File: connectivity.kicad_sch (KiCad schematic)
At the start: 28 parts, among them J10 Screw_Terminal_01x05, J11 RJ45_Hanrun_HR911105A_Horizon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, J8 Conn_02x01, J9 Conn_02x01, U10 LAN8742A, U9 TJA1042T-3, Y3 25 MHz

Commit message: Initial release A1
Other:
- note removed: "Re-check crystal footprint when crystal is chosen"
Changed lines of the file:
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@@
 	(title_block
 		(title "PT DAQ")
-		(date "2026-01-01")
+		(date "2026-01-12")
 		(rev "1A")
 		(company "Aggie Propulsion and Rocketry Lab")
@@
 	(text "ETH PHY"
 		(exclude_from_sim no)
-		(at 26.67 19.05 0)
+		(at 30.226 20.828 0)
 		(effects
 			(font
@@
 		)
 	)
-	(text "Re-check crystal footprint when crystal is chosen"
-		(exclude_from_sim no)
-		(at 45.72 119.38 0)
-		(effects
-			(font
-				(size 1.27 1.27)
-			)
-		)
-	)
 	(text "CAN"
 		(exclude_from_sim no)
@@
 		(dnp no)
 		(property "Reference" "Y3"
-			(at 45.212 118.872 0)
+			(at 48.006 119.634 0)
 			(effects
 				(font
@@
 		)
 		(property "Value" "25 MHz"
-			(at 46.228 121.92 0)
+			(at 49.022 122.682 0)
 			(effects
 				(font

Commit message: Pranked by propfeed and engine again
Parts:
- renumbered C38 to C32, C40 to C33, C42 to C34, C43 to C35, C37 to C36, C44 to C37, C45 to C38, C36 to C39, C46 to C40, C39 to C41, C41 to C42, R17 to R21, R18 to R22, R20 to R23, R21 to R24, R23 to R25, R24 to R26, R22 to R27, R19 to R28, R26 to R29, R25 to R30, U9 to U5, U10 to U6

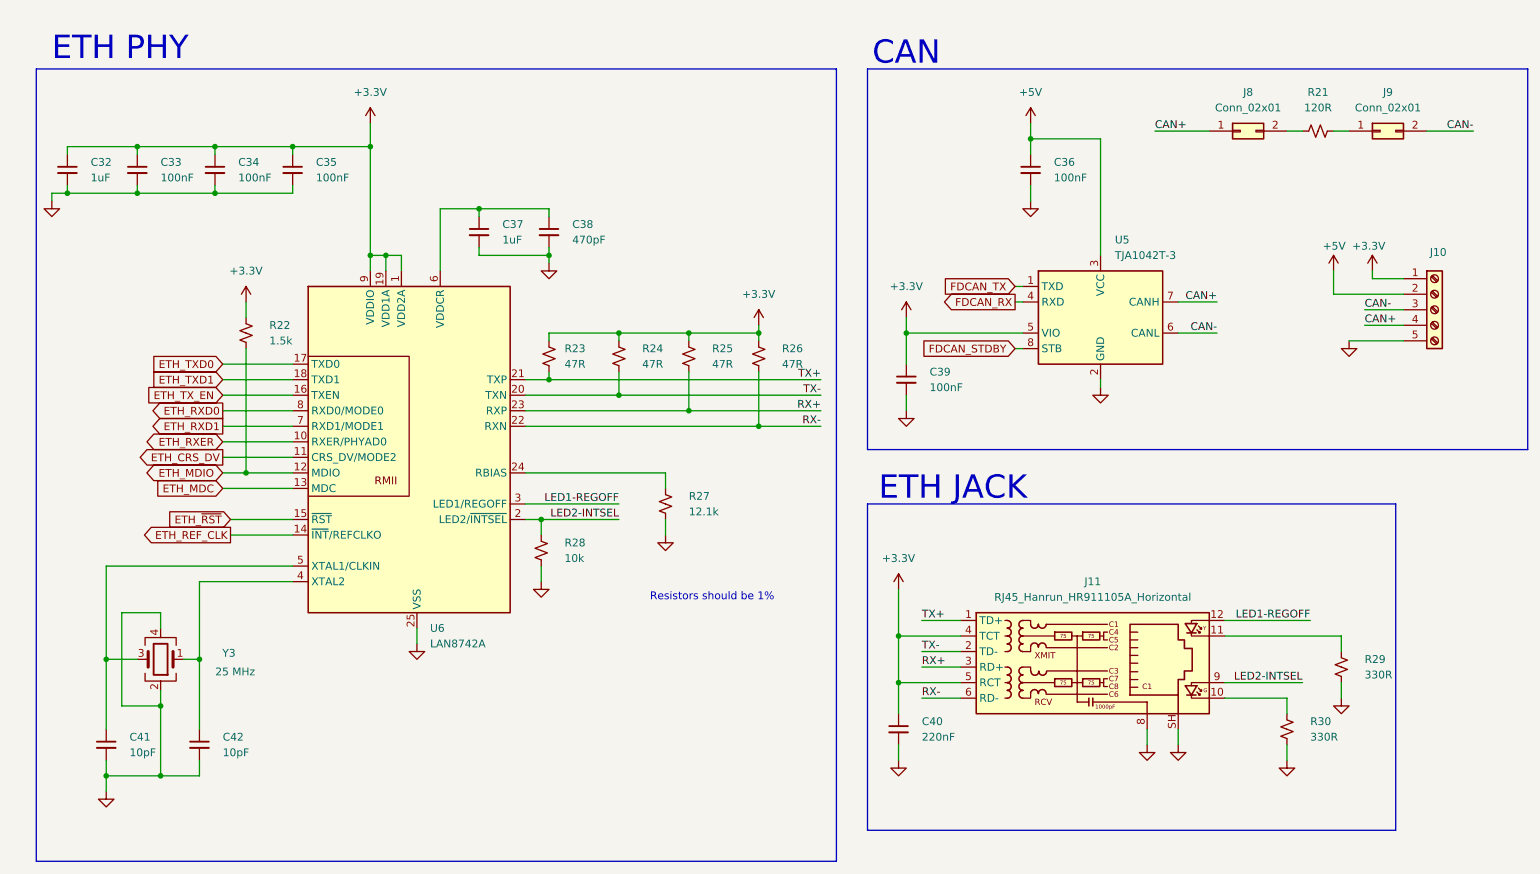
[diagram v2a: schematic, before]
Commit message: Swap TPS7A20 for LP5907 (Daniel yelled at me again)
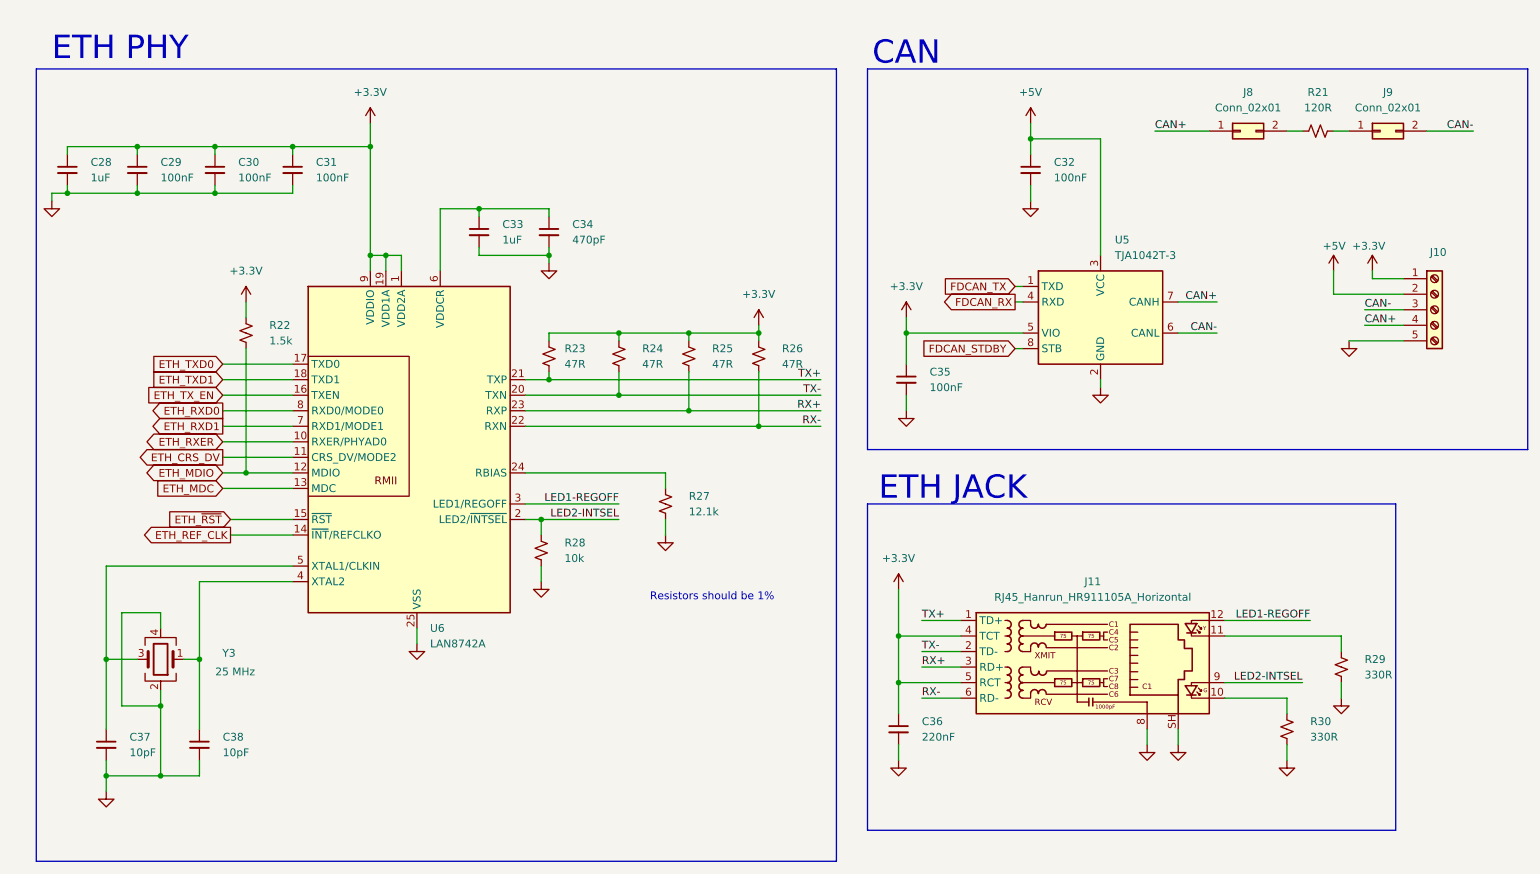
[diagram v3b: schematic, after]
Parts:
- renumbered C32 to C28, C33 to C29, C34 to C30, C35 to C31, C36 to C32, C37 to C33, C38 to C34, C39 to C35, C40 to C36, C41 to C37, C42 to C38
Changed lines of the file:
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@@
 		(dnp no)
 		(fields_autoplaced yes)
-		(property "Reference" "C36"
+		(property "Reference" "C32"
 			(at 182.88 39.3762 0)
 			(show_name no)
@@
 			(project "PT"
 				(path "/0eb5ae8a-84ea-4b7e-bec4-bb4e0217d666/c277875e-7a4a-49a6-a853-f4b1010be12e"
-					(reference "C36")
+					(reference "C32")
 					(unit 1)
 				)
@@
 		(dnp no)
 		(fields_autoplaced yes)
-		(property "Reference" "C41"
+		(property "Reference" "C37"
 			(at 31.75 133.3562 0)
 			(show_name no)
@@
 			(project "PT"
 				(path "/0eb5ae8a-84ea-4b7e-bec4-bb4e0217d666/c277875e-7a4a-49a6-a853-f4b1010be12e"
-					(reference "C41")
+					(reference "C37")
 					(unit 1)
 				)
@@
 		(dnp no)
 		(fields_autoplaced yes)
-		(property "Reference" "C32"
+		(property "Reference" "C28"
 			(at 25.4 39.3762 0)
 			(show_name no)
@@
 			(project "PT"
 				(path "/0eb5ae8a-84ea-4b7e-bec4-bb4e0217d666/c277875e-7a4a-49a6-a853-f4b1010be12e"
-					(reference "C32")
+					(reference "C28")
 					(unit 1)
 				)
@@
 		(dnp no)
 		(fields_autoplaced yes)
-		(property "Reference" "C37"
+		(property "Reference" "C33"
 			(at 92.71 49.5362 0)
 			(show_name no)
@@
 			(project "PT"
 				(path "/0eb5ae8a-84ea-4b7e-bec4-bb4e0217d666/c277875e-7a4a-49a6-a853-f4b1010be12e"
-					(reference "C37")
+					(reference "C33")
 					(unit 1)
 				)
@@
 		(dnp no)
 		(fields_autoplaced yes)
-		(property "Reference" "C33"
+		(property "Reference" "C29"
 			(at 36.83 39.3762 0)
 			(show_name no)
@@
 			(project "PT"
 				(path "/0eb5ae8a-84ea-4b7e-bec4-bb4e0217d666/c277875e-7a4a-49a6-a853-f4b1010be12e"
-					(reference "C33")
+					(reference "C29")
 					(unit 1)
 				)
@@
 		(dnp no)
 		(fields_autoplaced yes)
-		(property "Reference" "C35"
+		(property "Reference" "C31"
 			(at 62.23 39.3762 0)
 			(show_name no)
@@
 			(project "PT"
 				(path "/0eb5ae8a-84ea-4b7e-bec4-bb4e0217d666/c277875e-7a4a-49a6-a853-f4b1010be12e"
-					(reference "C35")
+					(reference "C31")
 					(unit 1)
 				)
@@
 		(dnp no)
 		(fields_autoplaced yes)
-		(property "Reference" "C40"
+		(property "Reference" "C36"
 			(at 161.29 130.8162 0)
 			(show_name no)
@@
 			(project "PT"
 				(path "/0eb5ae8a-84ea-4b7e-bec4-bb4e0217d666/c277875e-7a4a-49a6-a853-f4b1010be12e"
-					(reference "C40")
+					(reference "C36")
 					(unit 1)
 				)
@@
 		(dnp no)
 		(fields_autoplaced yes)
-		(property "Reference" "C38"
+		(property "Reference" "C34"
 			(at 104.14 49.5362 0)
 			(show_name no)
@@
 			(project "PT"
 				(path "/0eb5ae8a-84ea-4b7e-bec4-bb4e0217d666/c277875e-7a4a-49a6-a853-f4b1010be12e"
-					(reference "C38")
+					(reference "C34")
 					(unit 1)
 				)
@@
 		(dnp no)
 		(fields_autoplaced yes)
-		(property "Reference" "C42"
+		(property "Reference" "C38"
 			(at 46.99 133.3562 0)
 			(show_name no)
@@
 			(project "PT"
 				(path "/0eb5ae8a-84ea-4b7e-bec4-bb4e0217d666/c277875e-7a4a-49a6-a853-f4b1010be12e"
-					(reference "C42")
+					(reference "C38")
 					(unit 1)
 				)
@@
 		(dnp no)
 		(fields_autoplaced yes)
-		(property "Reference" "C34"
+		(property "Reference" "C30"
 			(at 49.53 39.3762 0)
 			(show_name no)
@@
 			(project "PT"
 				(path "/0eb5ae8a-84ea-4b7e-bec4-bb4e0217d666/c277875e-7a4a-49a6-a853-f4b1010be12e"
-					(reference "C34")
+					(reference "C30")
 					(unit 1)
 				)
@@
 		(dnp no)
 		(fields_autoplaced yes)
-		(property "Reference" "C39"
+		(property "Reference" "C35"
 			(at 162.56 73.6662 0)
 			(show_name no)
@@
 			(project "PT"
 				(path "/0eb5ae8a-84ea-4b7e-bec4-bb4e0217d666/c277875e-7a4a-49a6-a853-f4b1010be12e"
-					(reference "C39")
+					(reference "C35")
 					(unit 1)
 				)

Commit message: June 20th is not real and cant hurt me
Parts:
- C34: renamed from C28; footprint aprlprints:C_0603-noct -> APRLPrints:C_0603
- C35: renamed from C29; footprint aprlprints:C_0603-noct -> APRLPrints:C_0603
- C36: renamed from C30; footprint aprlprints:C_0603-noct -> APRLPrints:C_0603
- C37: renamed from C31; footprint aprlprints:C_0603-noct -> APRLPrints:C_0603
- C38: renamed from C32; footprint aprlprints:C_0603-noct -> APRLPrints:C_0603
- C39: renamed from C33; footprint aprlprints:C_0603-noct -> APRLPrints:C_0603
- C40: renamed from C34; footprint aprlprints:C_0603-noct -> APRLPrints:C_0603
- C41: renamed from C35; footprint aprlprints:C_0603-noct -> APRLPrints:C_0603
- C42: renamed from C36; footprint aprlprints:C_0603-noct -> APRLPrints:C_0603
- C43: renamed from C37; footprint aprlprints:C_0603-noct -> APRLPrints:C_0603
- C44: renamed from C38; footprint aprlprints:C_0603-noct -> APRLPrints:C_0603
- R21, R22, R23, R24, R25, R26, R27, R28, R29, R30: footprint aprlprints:R_0603-noct -> APRLPrints:R_0603
- Y3: footprint aprlprints:3225-4P-L-noct -> APRLPrints:3225-4P-L
- renumbered U5 to U6, U6 to U7

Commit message: Timeline is not real
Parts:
- added R31: 10k, APRLPrints:R_0603, symbol Device:R_Small_US
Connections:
- net GND: now also R31.1
- net ETH_RXER: no longer names the net of U7.10 (RXER/PHYAD0)
- net ETH_RXER: now also R31.2
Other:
- moved on the sheet: R22, R23, R24, R25, R26

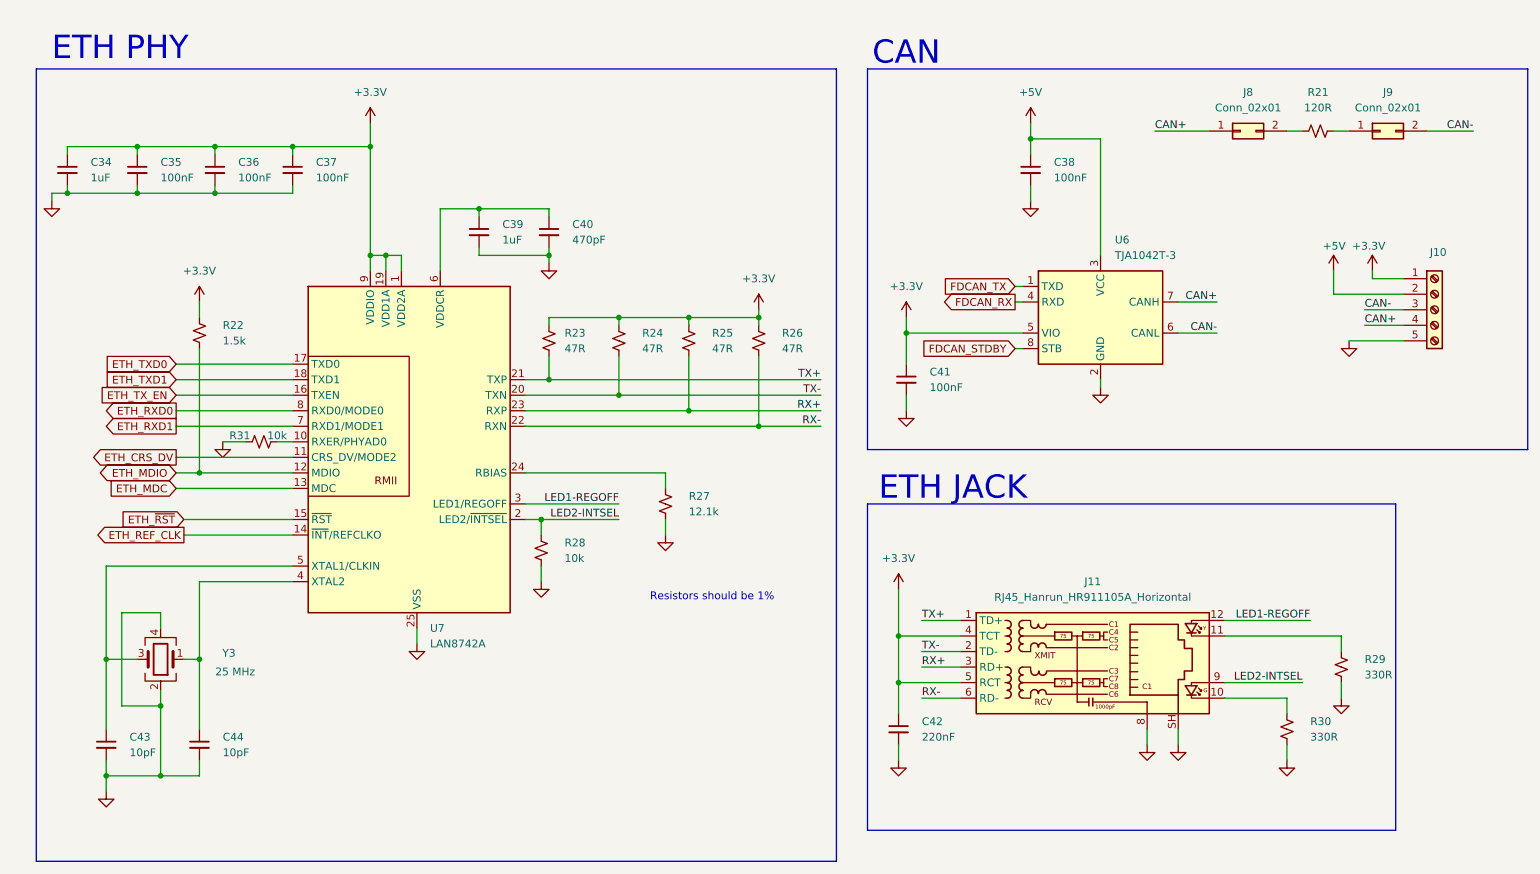
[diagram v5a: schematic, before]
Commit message: Remove LP5907
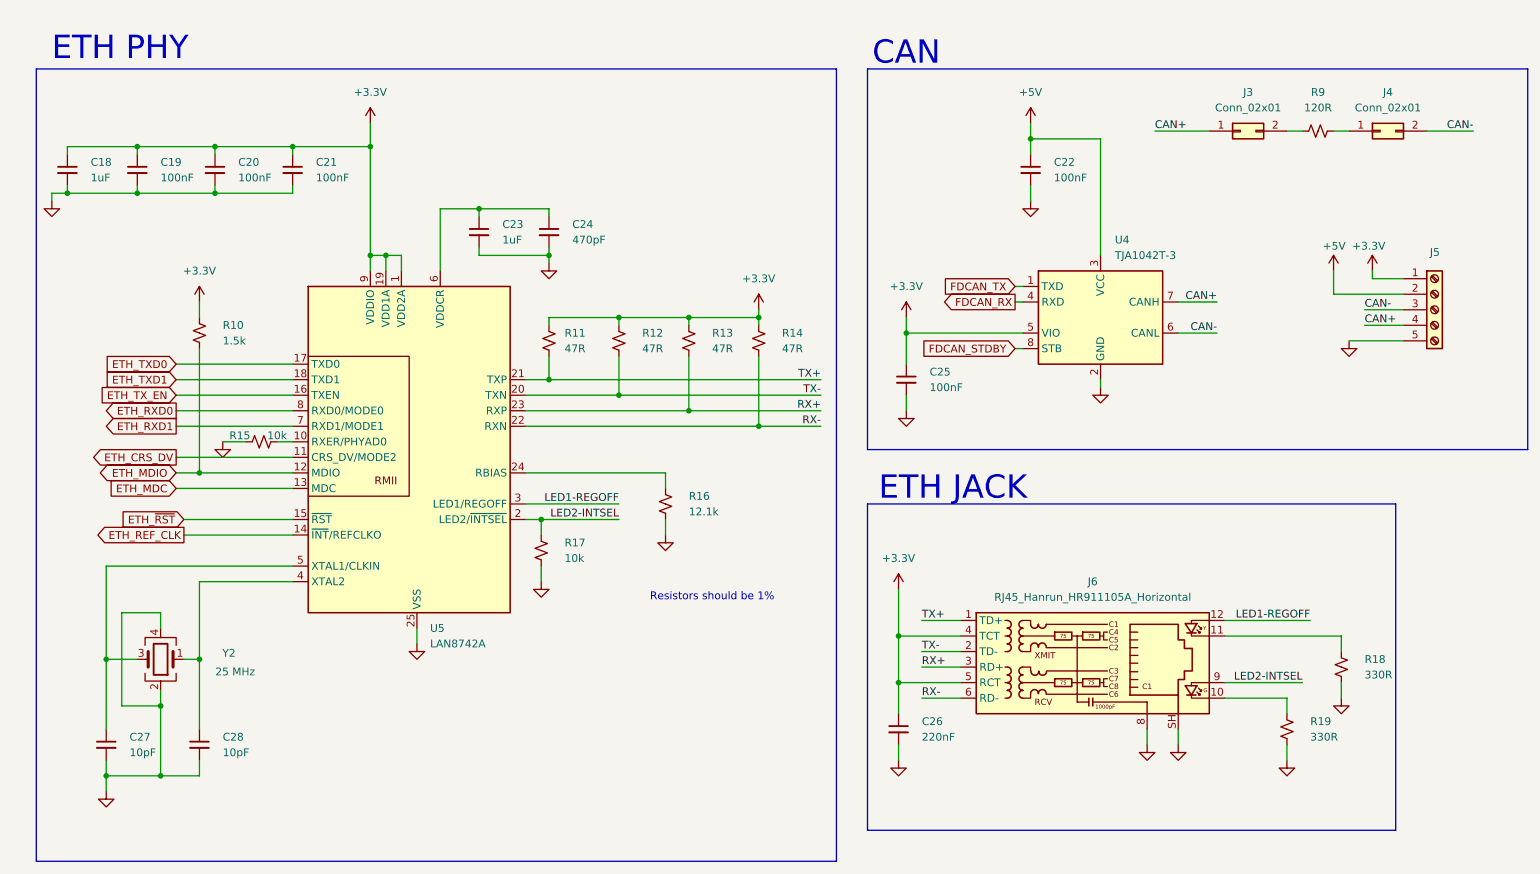
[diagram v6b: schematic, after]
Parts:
- renumbered C34 to C18, C35 to C19, C36 to C20, C37 to C21, C38 to C22, C39 to C23, C40 to C24, C41 to C25, C42 to C26, C43 to C27, C44 to C28, J8 to J3, J9 to J4, J10 to J5, J11 to J6, R22 to R10, R23 to R11, R24 to R12, R25 to R13, R26 to R14, R31 to R15, R27 to R16, R28 to R17, R29 to R18, R30 to R19, R21 to R9, U6 to U4, U7 to U5, Y3 to Y2
